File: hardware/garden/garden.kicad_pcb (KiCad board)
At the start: 4 copper layers, 80 x 51.5 mm, 83 parts, among them J1 CONN_01X04, J10 CONN_01X08, J11 CONN_01X02, J12 CONN_01X02, J2 CONN_01X02, J3 CONN_01X02, J4 CONN_01X02, J5 CONN_01X02, J6 CONN_01X02, J7 CONN_01X04, J8 CONN_01X04, J9 USB_C_Receptacle_USB2.0, Q1 Q_NPN_BEC, Q2 AO3416, Q3 AO3416, Q4 Q_NPN_BEC, Q5 Q_NMOS_GSD/30V, Q6 AO3416, Q7 AO3416, SW1 SW_Push, U1 INA226, U2 INA226, U3 CH340C, U4 ESP32-WROOM-32, U7 MCP1416, U9 MP2359

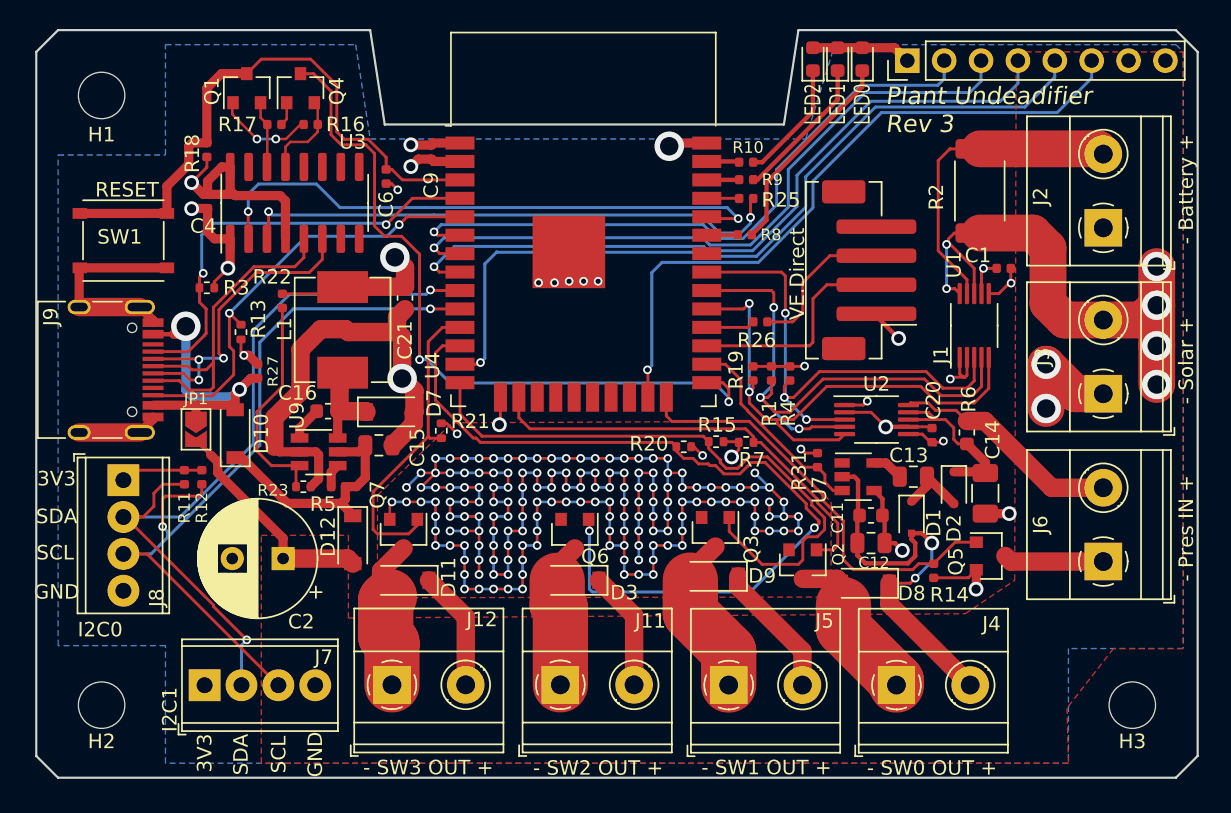
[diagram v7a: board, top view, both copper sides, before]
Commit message: Updated garden controller hardware to version 4
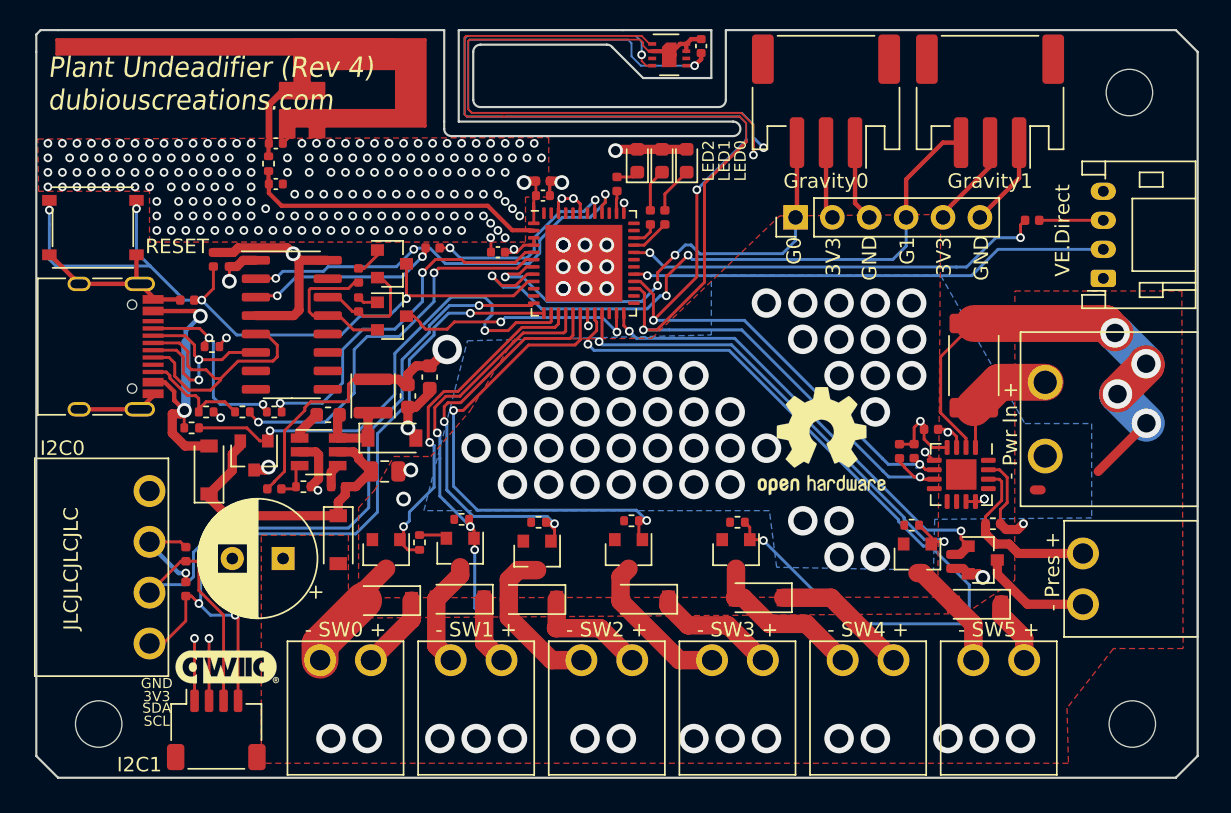
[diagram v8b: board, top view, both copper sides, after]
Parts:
- removed C11: 0.1uF/50V, Capacitor_SMD:C_0603_1608Metric
- removed C12, C13: 1uF/50V, Capacitor_SMD:C_0805_2012Metric
- removed C14: 10uF/50V, Capacitor_SMD:C_1206_3216Metric
- removed D1, D2: 1N4148, Diode_SMD:D_SOD-323F
- removed JP1: SolderJumper_2_Open, Jumper:SolderJumper-2_P1.3mm_Open_TrianglePad1.0x1.5mm
- removed R31: 10kR, Resistor_SMD:R_0402_1005Metric
- removed U4: ESP32-WROOM-32, RF_Module:ESP32-WROOM-32
- removed U7: MCP1416, Package_TO_SOT_SMD:SOT-23-5
- added AE1: Antenna_Dipole, Antennas:TI_DN007_2.4GHz, F.Cu at (76.6, 53.2)
- added C10: 22uF, Capacitor_SMD:C_0603_1608Metric, F.Cu at (80.6, 73.4)
- added C3: 0.1uF, Capacitor_SMD:C_0402_1005Metric, F.Cu at (88.4, 60.9)
- added C5: 0.1uF, Capacitor_SMD:C_0402_1005Metric, F.Cu at (85.3, 64.8)
- added C7: DNP, Capacitor_SMD:C_0402_1005Metric, F.Cu at (70.0, 57.3)
- added C8: 0.1uF, Capacitor_SMD:C_0402_1005Metric, F.Cu at (99.3, 50.6)
- added D13: D_Schottky, Diode_SMD:D_SOD-123, F.Cu at (103.3, 88.6)
- added D14: D_Schottky, Diode_SMD:D_SOD-123, F.Cu at (118.3, 89.0)
- added J13: CONN_01X02, modular_blocks:KF2EDGR-3.5-2P, F.Cu at (119.8, 100.8)
- added J14: CONN_01X03, Connector_JST:JST_PH_S3B-PH-SM4-TB_1x03-1MP_P2.00mm_Horizontal, F.Cu at (107.9, 54.4)
- added J16: CONN_01X03, Connector_JST:JST_PH_S3B-PH-SM4-TB_1x03-1MP_P2.00mm_Horizontal, F.Cu at (119.2, 54.4)
- added LOGO1: LOGO, Logos:qwiic, F.Cu at (66.6, 93.3)
- added LOGO2: Logo_Open_Hardware_Large, Symbol:OSHW-Logo2_9.8x8mm_SilkScreen, F.Cu at (107.6, 77.8)
- added Q10: YJL3416A, Package_TO_SOT_SMD:SOT-23, F.Cu at (114.2, 85.9)
- added Q8: Q_PMOS_GDS, Package_TO_SOT_SMD:SOT-23, F.Cu at (68.5, 78.8)
- added Q9: YJL3416A, Package_TO_SOT_SMD:SOT-23, F.Cu at (101.7, 85.6)
- added R24: 1kR, Resistor_SMD:R_0402_1005Metric, F.Cu at (64.2, 76.9)
- added R28: 100kR, Resistor_SMD:R_0402_1005Metric, F.Cu at (67.7, 75.8)
- added R29: 10kR, Resistor_SMD:R_0402_1005Metric, F.Cu at (101.8, 83.4)
- added R30: 10kR, Resistor_SMD:R_0402_1005Metric, F.Cu at (113.8, 83.6)
- added U6: ESP32-PICO-V3, Package_DFN_QFN:QFN-48-1EP_7x7mm_P0.5mm_EP5.3x5.3mm, F.Cu at (91.2, 65.6)
- C1: value 0.1uF -> DNP
- J1: footprint Connector_JST:JST_PH_B4B-PH-SM4-TB_1x04-1MP_P2.00mm_Vertical -> Connector_JST:JST_PH_S4B-PH-K_1x04_P2.00mm_Horizontal
- J10: value CONN_01X08 -> CONN_01X06; footprint Connector_PinHeader_2.54mm:PinHeader_1x08_P2.54mm_Vertical -> Connector_PinHeader_2.54mm:PinHeader_1x06_P2.54mm_Vertical
- J11, J12, J3, J4, J5, J6: footprint TerminalBlock_Phoenix:TerminalBlock_Phoenix_MKDS-1,5-2-5.08_1x02_P5.08mm_Horizontal -> modular_blocks:KF2EDGR-3.5-2P
- J2: footprint TerminalBlock_Phoenix:TerminalBlock_Phoenix_MKDS-1,5-2-5.08_1x02_P5.08mm_Horizontal -> modular_blocks:WJ2EDGRC-5-08-2P
- J7: footprint TerminalBlock_Phoenix:TerminalBlock_Phoenix_MPT-0,5-4-2.54_1x04_P2.54mm_Horizontal -> Connector_JST:JST_SH_SM04B-SRSS-TB_1x04-1MP_P1.00mm_Horizontal
- J8: footprint TerminalBlock_Phoenix:TerminalBlock_Phoenix_MPT-0,5-4-2.54_1x04_P2.54mm_Horizontal -> modular_blocks:KF2EDGR-3.5-4P
- L1: value 4.7uH -> 3.3uH; footprint MWSA0603:MWSA0603 -> Inductors:SWPA30xxS
- Q2, Q3, Q6, Q7: value AO3416 -> YJL3416A
- Q5: value Q_NMOS_GSD/30V -> Q_NMOS_GSD/60V
- R2: value 12mR -> 5mR
- R27: value 10kR -> 100kR
- R4: value 2.2kR -> 0R
- R6: value 2.2R -> 6.8R; footprint Resistor_SMD:R_0603_1608Metric -> Resistor_SMD:R_0402_1005Metric
- U1: value INA226 -> SHT30-DIS; footprint Package_SO:VSSOP-10_3x3mm_P0.5mm -> Sensor_Humidity:Sensirion_DFN-8-1EP_2.5x2.5mm_P0.5mm_EP1.1x1.7mm
- U2: value INA226 -> INA3221; footprint Package_SO:VSSOP-10_3x3mm_P0.5mm -> Package_DFN_QFN:Texas_RGV_S-PVQFN-N16_EP2.1x2.1mm
- U9: value MP2359 -> TPMP2359
- moved H1 70.8 mm to (128.8, 53.8)
- moved C1 50.5 mm to (70.0, 60.1), turned to 0 degrees
- moved R4 38.7 mm to (69.5, 58.7)
- moved J3 30.8 mm to (110.8, 100.8), turned to 0 degrees
- moved U1 28.1 mm to (97.1, 51.2), turned to 0 degrees
- moved R25 21.9 mm to (80.8, 64.5), turned to 0 degrees
- moved R26 20.0 mm to (122.1, 62.6)
- moved Q4 16.9 mm to (78.0, 69.2), turned to 0 degrees
- moved J1 16.1 mm to (127.0, 66.6)
- moved C6 16.1 mm to (63.9, 68.1), turned to 180 degrees
- moved R20 16.1 mm to (82.8, 83.2), turned to 0 degrees
- moved Q1 15.7 mm to (78.0, 65.6), turned to 0 degrees
- moved D8 15.3 mm to (95.4, 88.7)
- moved D4 14.0 mm to (98.3, 58.5)
- moved D5 14.0 mm to (96.6, 58.5)
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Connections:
- net Net-(C15-Pad1) renamed /Vbus_blocked
- C1 pad 1: +3V3 -> /LNA
- J10 pad 1: +3V3 -> /GRAVITY0
- J10 pad 2: /IO34 -> +3V3
- J10 pad 3: /IO35 -> GND
- J10 pad 4: /IO32 -> /GRAVITY1
- J10 pad 5: /IO14 -> +3V3
- J10 pad 6: /IO15 -> GND
- J3 pad 1: GND -> Net-(D13-Pad2)
- J6 pad 2: Net-(J6-Pad2) -> /PRES_SHUNT_N
- J7 pad 1: +3V3 -> GND
- J7 pad 2: /SDA_EXT -> +3V3
- J7 pad 3: /SCL_EXT -> /SDA_EXT
- J7 pad 4: GND -> /SCL_EXT
- J8 pad 1: +3V3 -> GND
- J8 pad 2: /SDA_EXT -> +3V3
- J8 pad 3: /SCL_EXT -> /SDA_EXT
- J8 pad 4: GND -> /SCL_EXT
- Q2 pad 1: /SW0 -> /SW3
- Q3 pad 1: /SW1 -> /SW2
- Q6 pad 1: /SW2 -> /SW1
- Q7 pad 1: /SW3 -> /SW0
- R15 pad 2: /SW1 -> /SW2
- R20 pad 2: /SW2 -> /SW1
- R21 pad 2: /SW3 -> /SW0
- R27 pad 1: GND -> /CC1
- R27 pad 2: /Vbus -> /CC1_ADC
- R4 pad 1: +3V3 -> Net-(AE1-Pad2)
- R4 pad 2: /ALERT -> /LNA
- R6 pad 1: Net-(J6-Pad2) -> /PRES_SHUNT_N
- R6 pad 2: Net-(C14-Pad1) -> +12V
- R7 pad 2: /SW0 -> /SW3
- U1 pad 1: GND -> /SDA
- U1 pad 3: /ALERT -> (no net)
- U1 pad 4: /SDA -> /SCL
- U1 pad 5: /SCL -> +3V3
- U1 pad 6: +3V3 -> (no net)
- U1 pad 8: +12V -> GND
- U1 pad 9: /BATT_SHUNT_N -> GND
- U2 pad 1: +3V3 -> /BATT_SHUNT_N
- U2 pad 10: Net-(J6-Pad2) -> (no net)
- U2 pad 2: GND -> +12V
- U2 pad 3: /ALERT -> GND
- U2 pad 4: /SDA -> +3V3
- U2 pad 5: /SCL -> GND
- U2 pad 6: +3V3 -> /SCL
- U2 pad 7: GND -> /SDA
- U2 pad 8: Net-(C14-Pad1) -> (no net)
- U2 pad 9: Net-(C14-Pad1) -> (no net)
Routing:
- net GND: track 289.4 -> 122.2 mm, vias 188 -> 253
- net +3V3: track 54.8 -> 128.0 mm, vias 7 -> 14
- net /SW4: track 0.00 -> 57.0 mm, vias 0 -> 2
- net /IO14: track 55.6 -> 0.00 mm, vias 1 -> 0
- net /IO32: track 50.5 -> 0.00 mm, vias 1 -> 0
- net /IO35: track 47.7 -> 0.00 mm, vias 1 -> 0
- net /IO15: track 46.9 -> 0.00 mm, vias 1 -> 0
- net /SCL: track 37.5 -> 83.7 mm, vias 2 -> 4
- net /SDA: track 40.1 -> 85.7 mm, vias 3 -> 2
- net /GRAVITY1: track 0.00 -> 45.2 mm, vias 0 -> 3
- net /IO34: track 44.9 -> 0.00 mm, vias 1 -> 0
- net /ALERT: track 36.1 -> 0.00 mm, vias 3 -> 0
- net /~Vbus_to_12V_EN: track 0.00 -> 34.3 mm, vias 0 -> 2
- net /SW5: track 0.00 -> 34.2 mm, vias 0 -> 2
- net /IO0: track 50.6 -> 17.0 mm
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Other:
- outline, holes or cut-outs redrawn
- net class Default: clearance 0.1778 -> 0.127
- rule trace_clearance: 0.1778 -> 0.127
- board text added: "- Pres +"
- board text added: "- Pwr In +"
- board text added: "- SW0 +"
- board text added: "- SW1 +"
- board text added: "- SW2 +"
- board text added: "- SW3 +"
- board text added: "- SW4 +"
- board text added: "- SW5 +"
- board text added: "G0"
- board text added: "G1"
- board text added: "Gravity0"
- board text added: "Gravity1"
- board text added: "JLCJLCJLCJLC"
- board text added: "Plant Undeadifier (Rev 4) dubiouscreations.com"
- board text removed: "- Battery +"
- board text removed: "- Pres IN +"
- board text removed: "- SW0 OUT +"
- board text removed: "- SW1 OUT +"
- board text removed: "- SW2 OUT +"
- board text removed: "- SW3 OUT +"
- board text removed: "- Solar +"
- board text removed: "Dubious Creations https://dubiouscreations.com"
- board text removed: "Plant Undeadifier Rev 3"
